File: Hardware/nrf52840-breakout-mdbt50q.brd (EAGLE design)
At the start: 47 x 22.9 mm, 105 parts, among them J8 CORTEX_DEBUG_PTH, U1 MDBT50Q, U2 MCP73831, U3 3.3V, Y1 32.768kHz

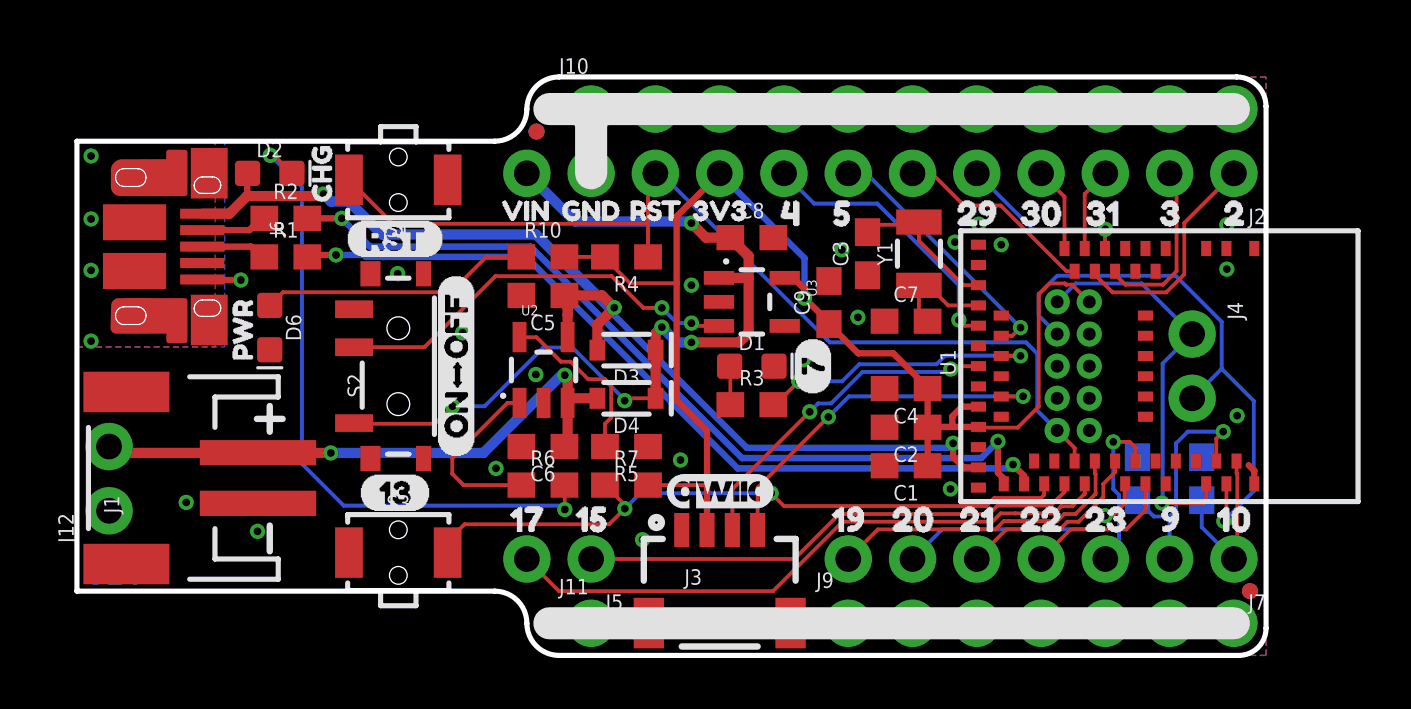
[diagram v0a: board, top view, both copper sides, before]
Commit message: Board revisions post engineer checklist
- Added extra ground PTH
- Added production sku for nRF module
- Added link to tutorial
- Clean up schematic
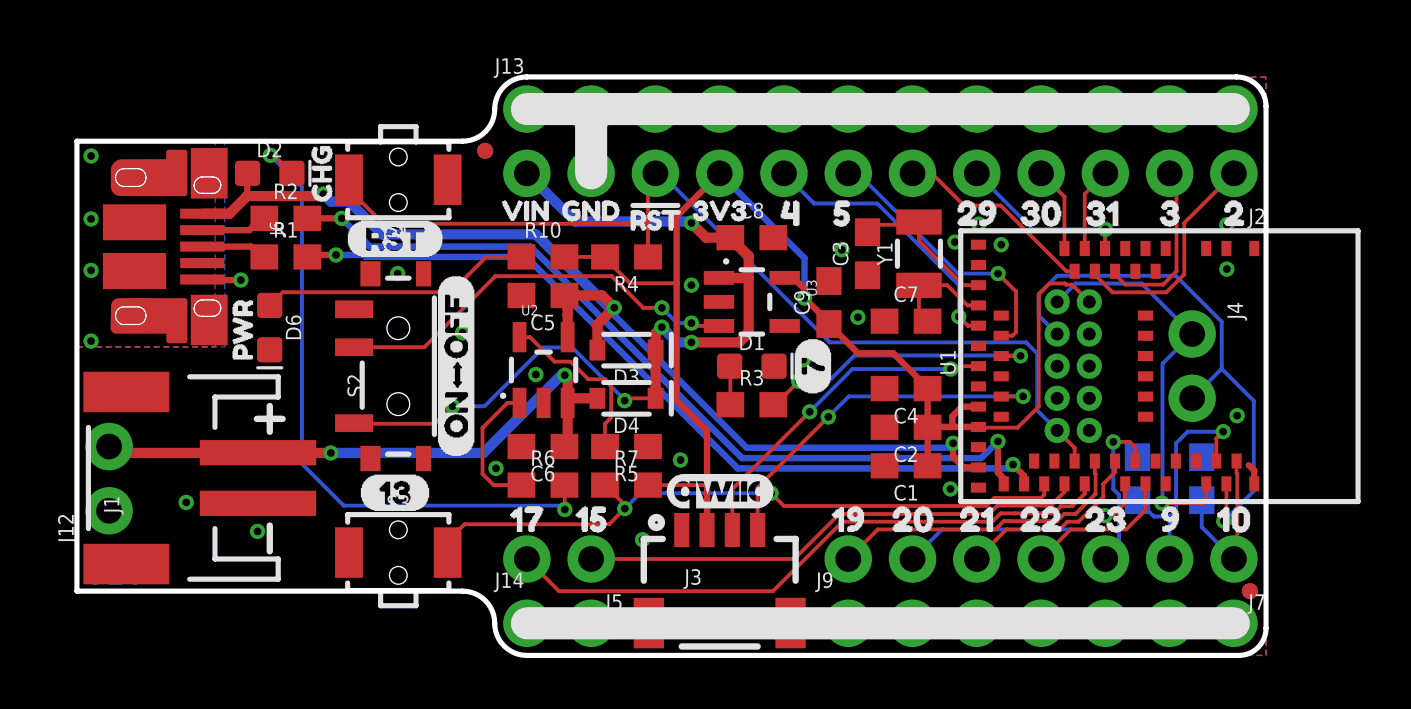
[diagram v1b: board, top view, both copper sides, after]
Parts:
- removed J10: (no value), SparkFun-Connectors:1X11_NO_SILK
- removed J11: (no value), SparkFun-Connectors:1X01_NO_SILK
- added J13: (no value), SparkFun-Connectors:1X12_NO_SILK
- added J14: (no value), SparkFun-Connectors:1X02_NO_SILK
- added U$17: (no value), buzzard_labels:HTTP###SFE#IO#T8200
- D1: value GREEN -> BLUE
- LOGO2: value OSHW-LOGOM -> OSHW-LOGOS; device SparkFun-Aesthetics:OSHW-LOGO-M -> SparkFun-Aesthetics:OSHW-LOGO-S
- moved LOGO2 12.3 mm to (2.54, 16.4), turned to 90 degrees
- moved FRAME1 11.4 mm to (2.54, -21.6)
- moved FD1 2.17 mm to (16.1, 19.9)
- moved FD4 2.17 mm to (16.1, 19.9)
- moved U$3 0.38 mm to (21.2, 17.2)
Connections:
- net GND: now also J13.1, J13.10, J13.11, J13.12, J13.2, J13.3, J13.4, J13.5, J13.6, J13.7, J13.8, J13.9, J14.1, J14.2; no longer J10.1, J10.10, J10.11, J10.2, J10.3, J10.4, J10.5, J10.6, J10.7, J10.8, J10.9, J11.1
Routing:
- net N$4: track 7.10 -> 5.41 mm
- net P0.05/AIN3: track 10.2 -> 10.8 mm
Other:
- outline, holes or cut-outs redrawn
- board text added: "Units in inches"

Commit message: Adding pull-up resistors to I2C lines.
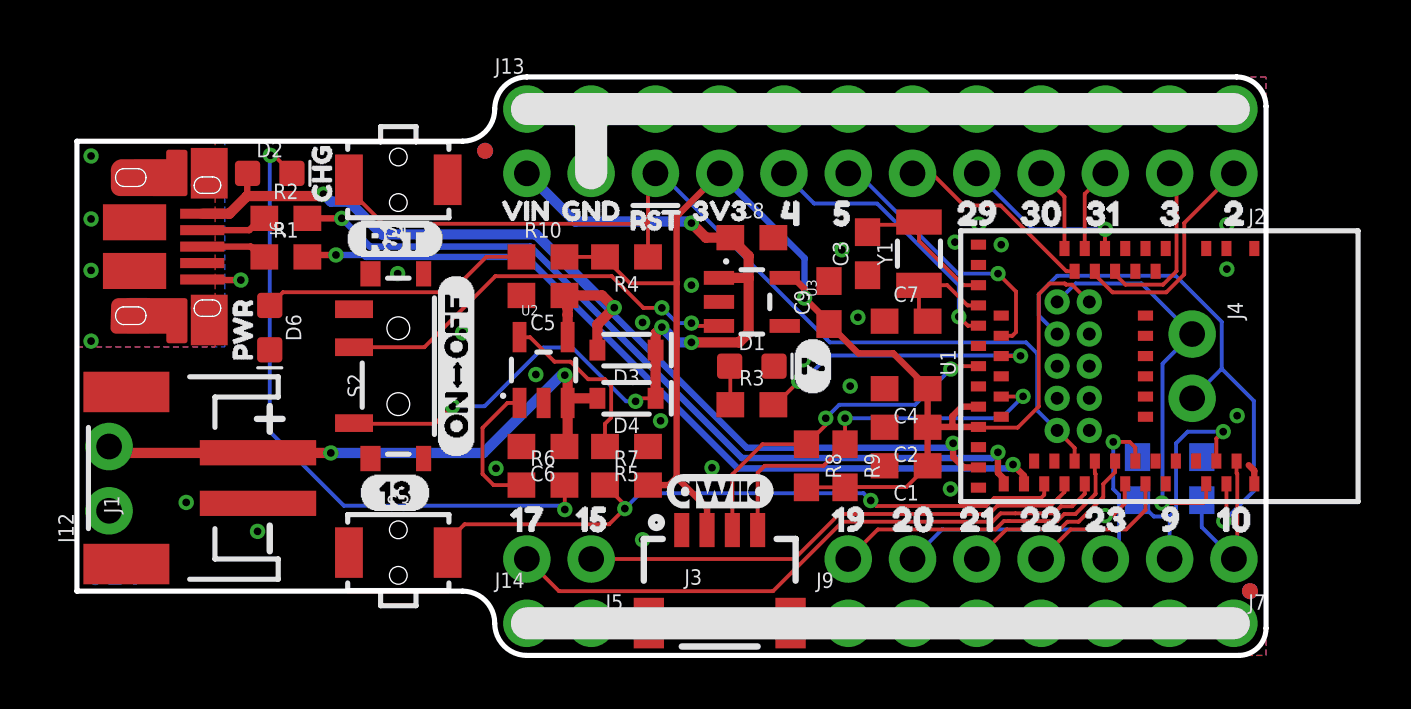
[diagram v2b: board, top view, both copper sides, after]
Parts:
- added R8, R9: 2.2k, SparkFun-Resistors:0603
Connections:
- net 3.3V: now also R8.2, R9.2
- net P0.08: now also R8.1
- net P0.11: now also R9.1
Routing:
- net 3.3V: track 52.9 -> 57.0 mm
- net P0.11: track 14.5 -> 15.5 mm
- net D-: track 33.3 -> 32.7 mm
- net GND: vias 20 -> 23

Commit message: Engineering review revisions
- Increase USB data line clearance to 10mil
- Move silkscreen to better-avoid stop
- Add silk to indicate ADC pins
- Minor trace re-routing
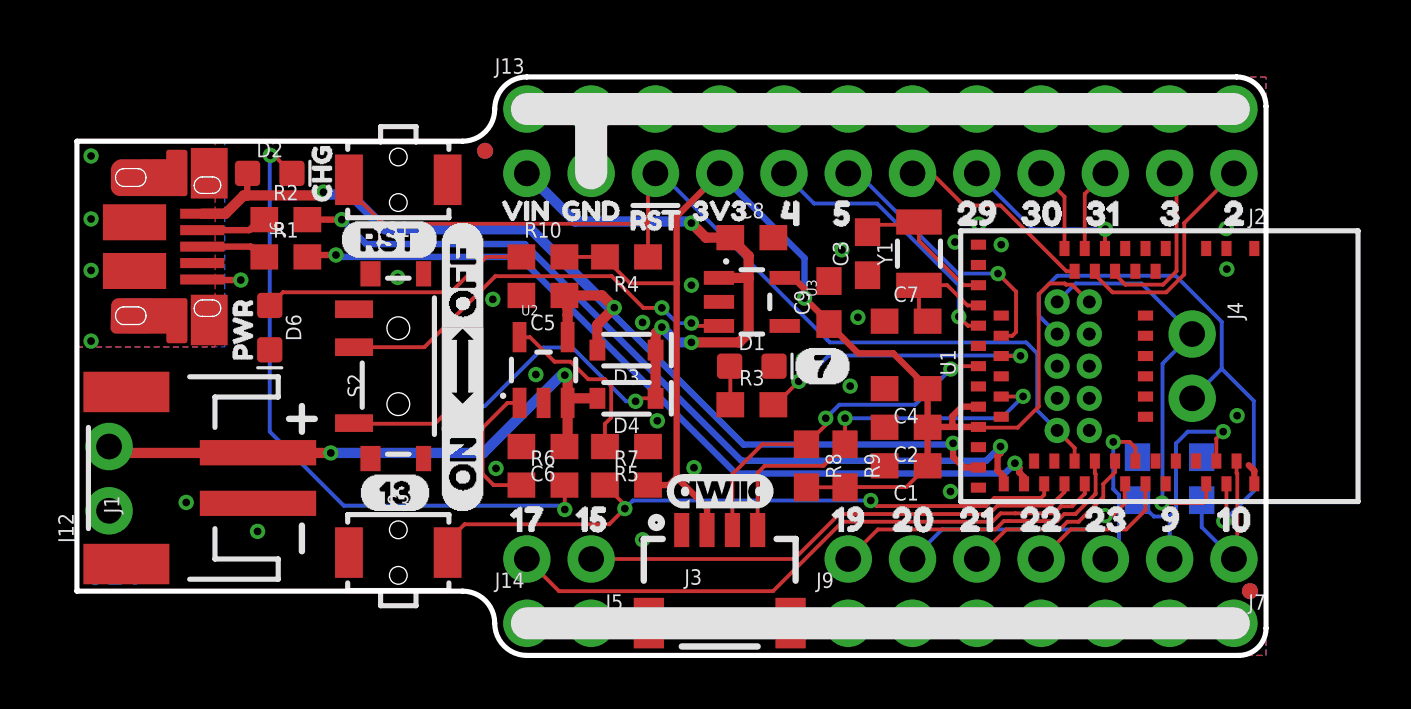
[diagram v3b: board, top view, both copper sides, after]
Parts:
- added U$52: (no value), buzzard_labels:ANALOG2
- added U$58: (no value), buzzard_labels:OFF2
- U$36: device buzzard_labels:304 -> buzzard_labels:301
- U$4: device buzzard_labels:ON#OFF4 -> buzzard_labels:ON1
- moved U$35 5.08 mm to (33.0, 15.0)
- moved U$33 4.83 mm to (45.8, 9.53), turned to 90 degrees
- moved U$11 2.54 mm to (38.1, 15.0)
- moved U$14 2.54 mm to (35.6, 15.0)
- moved U$4 2.20 mm to (15.2, 5.59)
- moved U$57 2.11 mm to (42.5, 8.38), turned to 90 degrees
- moved U$56 1.62 mm to (42.5, 11.6), turned to 90 degrees
- moved U$28 1.37 mm to (28.3, 11.4), turned to 0 degrees
- moved U$51 0.23 mm to (10.4, 16.4)
- moved R2 0.05 mm to (8.26, 17.2)
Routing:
- net D-: track 32.7 -> 33.2 mm
